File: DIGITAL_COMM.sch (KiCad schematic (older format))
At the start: 7 parts, among them U4 MCP3004, U5 TC77

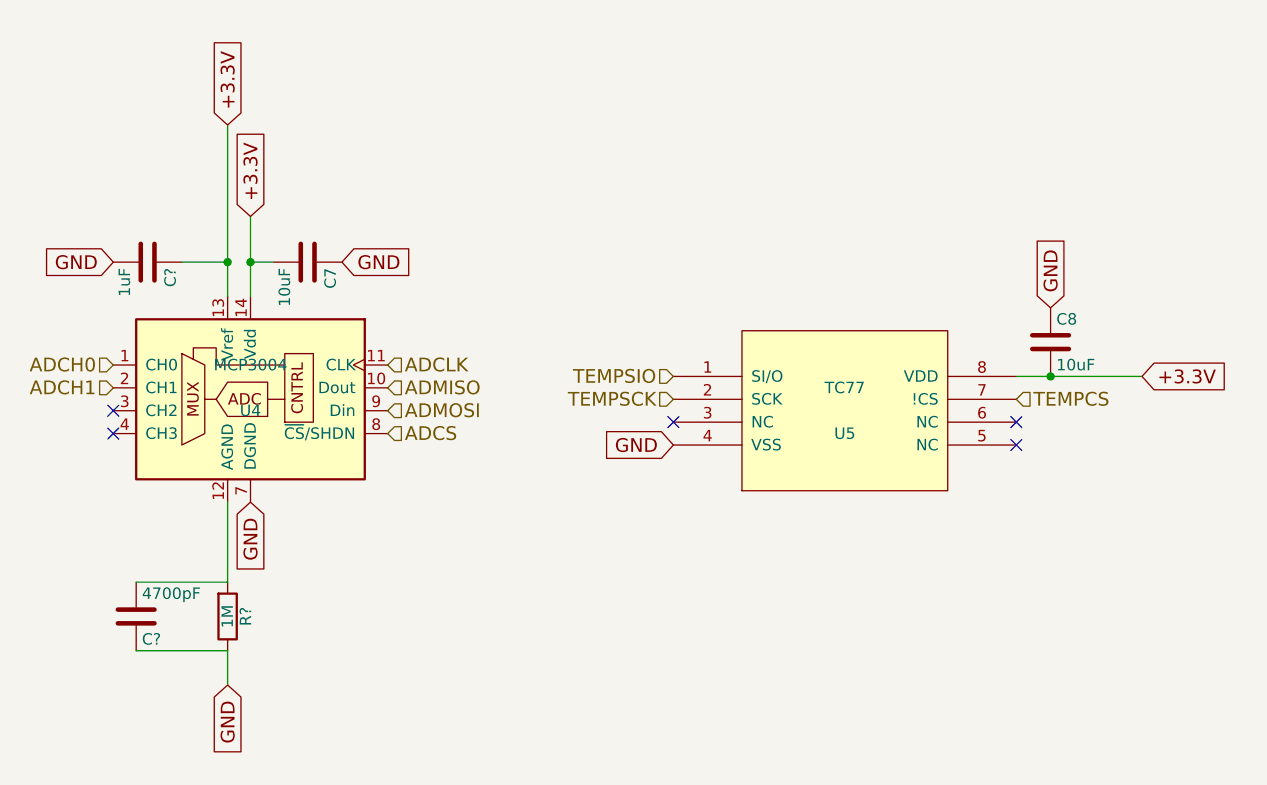
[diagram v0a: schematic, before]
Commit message: this version contains the datasheets and the footprints of the parts
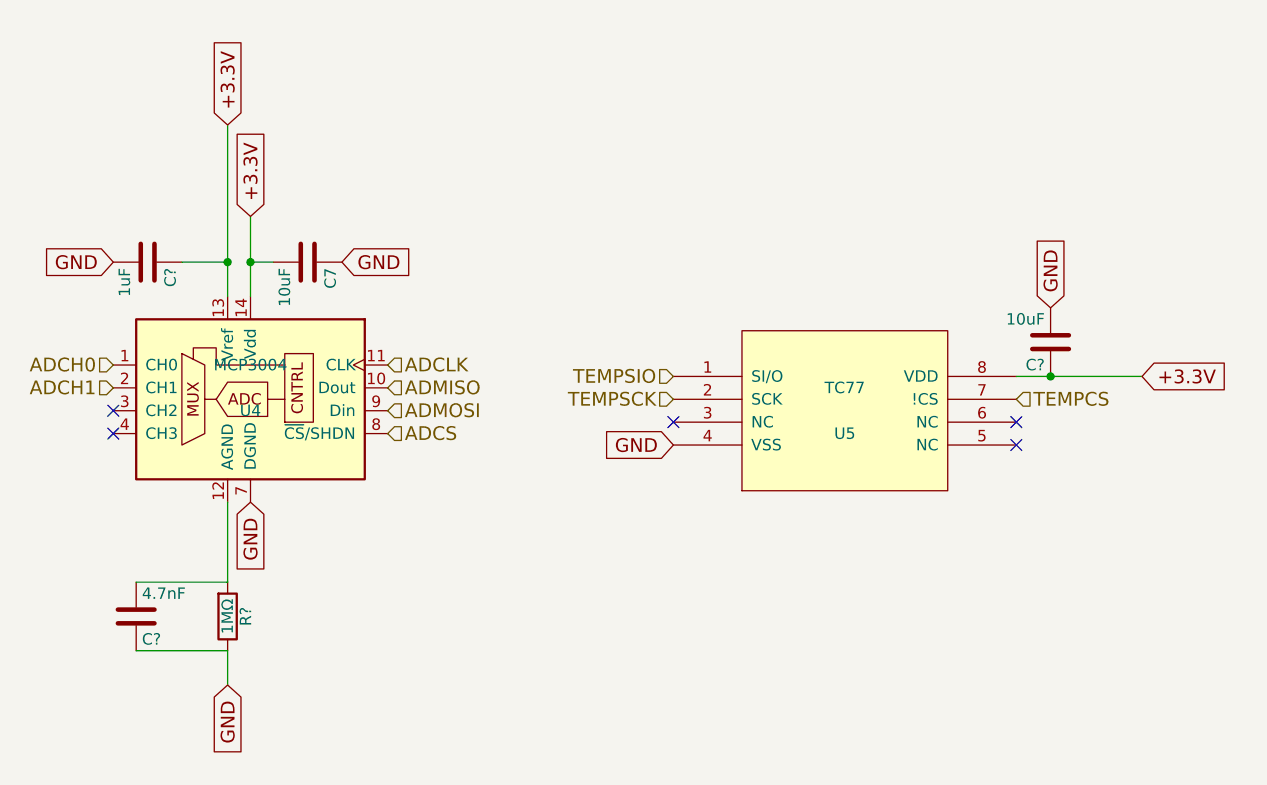
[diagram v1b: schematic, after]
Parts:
- removed C8: 10uF, Capacitors_SMD:C_1206_HandSoldering, symbol C
- removed C?: 4700pF, symbol C
- added C?: 4.7nF, Capacitors_SMD:C_0603_HandSoldering, symbol C
- added C?: 10uF, Capacitors_SMD:C_0603_HandSoldering, symbol C
- C7: footprint Capacitors_SMD:C_1206_HandSoldering -> Capacitors_SMD:C_0603_HandSoldering; avx (none) -> http://hu.farnell.com/avx/06036d106mat2a/cap-mlcc-x5r-10uf-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
- C?: footprint (none) -> Capacitors_SMD:C_0603_HandSoldering
- R?: value 1M -> 1MΩ; footprint (none) -> Resistors_SMD:R_0603_HandSoldering
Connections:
- net +3.3V: now also C?.1
- net GND: now also C?.1, C?.2
- net at R?.2, U4.12 (AGND): now also C?.2
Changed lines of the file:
@@
-$EndComp
-$Comp
-L C C8
-U 1 1 561C1F39
-P 7050 2400
-F 0 "C8" H 7075 2500 50  0000 L CNN
-F 1 "10uF" H 7075 2300 50  0000 L CNN
-F 2 "Capacitors_SMD:C_1206_HandSoldering" H 7088 2250 30  0001 C CNN
-F 3 "" H 7050 2400 60  0000 C CNN
-	1    7050 2400
-	1    0    0    -1
 $EndComp
 $Comp
@@
 F 0 "C7" H 3825 2150 50  0000 L CNN
 F 1 "10uF" H 3825 1950 50  0000 L CNN
-F 2 "Capacitors_SMD:C_1206_HandSoldering" H 3838 1900 30  0001 C CNN
-F 3 "" H 3800 2050 60  0000 C CNN
+F 2 "Capacitors_SMD:C_0603_HandSoldering" H 3838 1900 30  0001 C CNN
+F 3 "http://hu.farnell.com/murata/grm188r60g106me47d/cap-mlcc-x5r-10uf-4v-0603/dp/2688517" H 3800 2050 60  0001 C CNN
+F 4 "http://hu.farnell.com/avx/06036d106mat2a/cap-mlcc-x5r-10uf-6-3v-0603/dp/1833804" H 3800 2050 60  0001 C CNN "avx"
 	1    3800 2050
 	0    1    1    0
@@
 GND
 $Comp
-L C C?
-U 1 1 59A60423
-P 3050 3600
-F 0 "C?" H 3075 3700 50  0000 L CNN
-F 1 "4700pF" H 3075 3500 50  0000 L CNN
-F 2 "" H 3088 3450 50  0001 C CNN
-F 3 "" H 3050 3600 50  0001 C CNN
-	1    3050 3600
-	1    0    0    1
-$EndComp
-$Comp
 L R R?
 U 1 1 59A6042A
 P 3450 3600
 F 0 "R?" V 3530 3600 50  0000 C CNN
-F 1 "1M" V 3450 3600 50  0000 C CNN
-F 2 "" V 3380 3600 50  0001 C CNN
-F 3 "" H 3450 3600 50  0001 C CNN
+F 1 "1MΩ" V 3450 3600 50  0000 C CNN
+F 2 "Resistors_SMD:R_0603_HandSoldering" V 3380 3600 50  0001 C CNN
+F 3 "http://hu.farnell.com/multicomp/mcwr06x1004ftl/res-thick-film-1m-1-0-1w-0603/dp/2447285" H 3450 3600 50  0001 C CNN
 	1    3450 3600
 	1    0    0    1
@@
 F 0 "C?" H 3125 2150 50  0000 L CNN
 F 1 "1uF" H 3125 1950 50  0000 L CNN
-F 2 "" H 3138 1900 50  0001 C CNN
-F 3 "" H 3100 2050 50  0001 C CNN
+F 2 "Capacitors_SMD:C_0603_HandSoldering" H 3138 1900 50  0001 C CNN
+F 3 "http://hu.farnell.com/avx/0603zd105kat2a/cap-mlcc-x5r-1uf-10v-0603/dp/1327684" H 3100 2050 50  0001 C CNN
 	1    3100 2050
 	0    1    1    0
@@
 NoConn ~ 2950 2800
 NoConn ~ 2950 2700
+$Comp
+L C C?
+U 1 1 59A7620E
+P 7050 2400
+F 0 "C?" H 7075 2500 50  0000 L CNN
+F 1 "10uF" H 7075 2300 50  0000 L CNN
+F 2 "Capacitors_SMD:C_0603_HandSoldering" H 7088 2250 30  0001 C CNN
+F 3 "http://hu.farnell.com/murata/grm188r60g106me47d/cap-mlcc-x5r-10uf-4v-0603/dp/2688517" H 7050 2400 60  0001 C CNN
+F 4 "http://hu.farnell.com/avx/06036d106mat2a/cap-mlcc-x5r-10uf-6-3v-0603/dp/1833804" H 7050 2400 60  0001 C CNN "avx"
+	1    7050 2400
+	-1   0    0    1
+$EndComp
+$Comp
+L C C?
+U 1 1 59A6A163
+P 3050 3600
+F 0 "C?" H 3075 3700 50  0000 L CNN
+F 1 "4.7nF" H 3075 3500 50  0000 L CNN
+F 2 "Capacitors_SMD:C_0603_HandSoldering" H 3088 3450 50  0001 C CNN
+F 3 "http://hu.farnell.com/avx/06035c472kat2a/cap-mlcc-x7r-4-7nf-50v-0603/dp/317263" H 3050 3600 50  0001 C CNN
+	1    3050 3600
+	1    0    0    1
+$EndComp
 $EndSCHEMATC

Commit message: some issues fixed by the bugfixer; formal verification needed
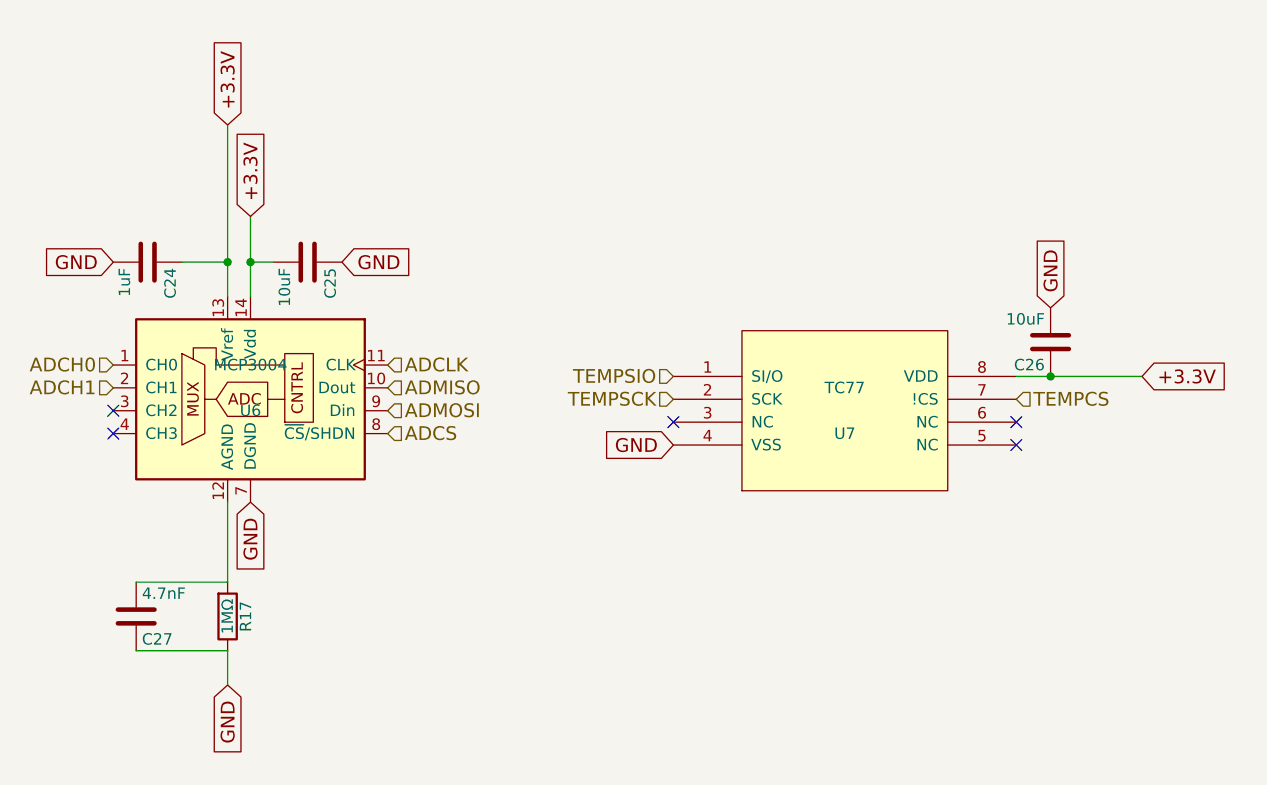
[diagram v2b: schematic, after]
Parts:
- gave numbers to parts that had none: 4
- renumbered C7 to C25, U4 to U6, U5 to U7
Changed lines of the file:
@@
 $EndDescr
 $Comp
-L MCP3004 U4
+L MCP3004 U6
 U 1 1 561B93E7
 P 3550 2600
-F 0 "U4" H 3550 2500 50  0000 C CNN
+F 0 "U6" H 3550 2500 50  0000 C CNN
 F 1 "MCP3004" H 3550 2700 50  0000 C CNN
 F 2 "Housings_SOIC:SOIC-14_3.9x8.7mm_Pitch1.27mm" H 3550 2600 50  0001 C CNN
@@
 $EndComp
 $Comp
-L TC77 U5
+L TC77 U7
 U 1 1 561B943C
 P 6150 2700
-F 0 "U5" H 6150 2600 50  0000 C CNN
+F 0 "U7" H 6150 2600 50  0000 C CNN
 F 1 "TC77" H 6150 2800 50  0000 C CNN
 F 2 "Housings_SOIC:SOIC-8_3.9x4.9mm_Pitch1.27mm" H 6150 2700 50  0001 C CNN
@@
 $EndComp
 $Comp
-L C C7
+L C C25
 U 1 1 561C1FA8
 P 3800 2050
-F 0 "C7" H 3825 2150 50  0000 L CNN
+F 0 "C25" H 3825 2150 50  0000 L CNN
 F 1 "10uF" H 3825 1950 50  0000 L CNN
 F 2 "Capacitors_SMD:C_0603_HandSoldering" H 3838 1900 30  0001 C CNN
@@
 GND
 $Comp
-L R R?
+L R R17
 U 1 1 59A6042A
 P 3450 3600
-F 0 "R?" V 3530 3600 50  0000 C CNN
+F 0 "R17" V 3530 3600 50  0000 C CNN
 F 1 "1MΩ" V 3450 3600 50  0000 C CNN
 F 2 "Resistors_SMD:R_0603_HandSoldering" V 3380 3600 50  0001 C CNN
@@
 	3450 3100 3450 3450
 $Comp
-L C C?
+L C C24
 U 1 1 59A609F8
 P 3100 2050
-F 0 "C?" H 3125 2150 50  0000 L CNN
+F 0 "C24" H 3125 2150 50  0000 L CNN
 F 1 "1uF" H 3125 1950 50  0000 L CNN
 F 2 "Capacitors_SMD:C_0603_HandSoldering" H 3138 1900 50  0001 C CNN
@@
 NoConn ~ 2950 2700
 $Comp
-L C C?
+L C C26
 U 1 1 59A7620E
 P 7050 2400
-F 0 "C?" H 7075 2500 50  0000 L CNN
+F 0 "C26" H 7075 2500 50  0000 L CNN
 F 1 "10uF" H 7075 2300 50  0000 L CNN
 F 2 "Capacitors_SMD:C_0603_HandSoldering" H 7088 2250 30  0001 C CNN
@@
 $EndComp
 $Comp
-L C C?
+L C C27
 U 1 1 59A6A163
 P 3050 3600
-F 0 "C?" H 3075 3700 50  0000 L CNN
+F 0 "C27" H 3075 3700 50  0000 L CNN
 F 1 "4.7nF" H 3075 3500 50  0000 L CNN
 F 2 "Capacitors_SMD:C_0603_HandSoldering" H 3088 3450 50  0001 C CNN

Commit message: part numbers generated;
pcb generation started
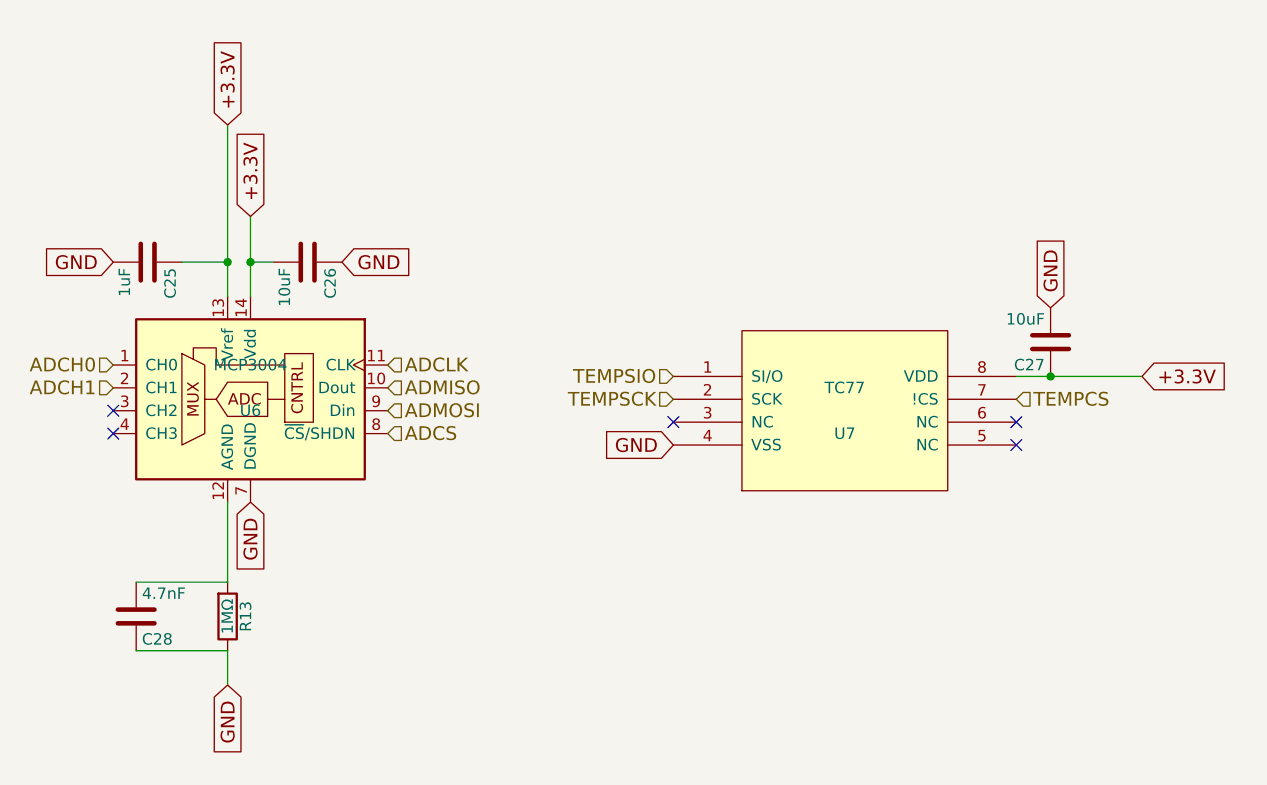
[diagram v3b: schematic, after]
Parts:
- renumbered C24 to C25, C25 to C26, C26 to C27, C27 to C28, R17 to R13
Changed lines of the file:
@@
 $EndComp
 $Comp
-L C C25
+L C C26
 U 1 1 561C1FA8
 P 3800 2050
-F 0 "C25" H 3825 2150 50  0000 L CNN
+F 0 "C26" H 3825 2150 50  0000 L CNN
 F 1 "10uF" H 3825 1950 50  0000 L CNN
 F 2 "Capacitors_SMD:C_0603_HandSoldering" H 3838 1900 30  0001 C CNN
@@
 GND
 $Comp
-L R R17
+L R R13
 U 1 1 59A6042A
 P 3450 3600
-F 0 "R17" V 3530 3600 50  0000 C CNN
+F 0 "R13" V 3530 3600 50  0000 C CNN
 F 1 "1MΩ" V 3450 3600 50  0000 C CNN
 F 2 "Resistors_SMD:R_0603_HandSoldering" V 3380 3600 50  0001 C CNN
@@
 	3450 3100 3450 3450
 $Comp
-L C C24
+L C C25
 U 1 1 59A609F8
 P 3100 2050
-F 0 "C24" H 3125 2150 50  0000 L CNN
+F 0 "C25" H 3125 2150 50  0000 L CNN
 F 1 "1uF" H 3125 1950 50  0000 L CNN
 F 2 "Capacitors_SMD:C_0603_HandSoldering" H 3138 1900 50  0001 C CNN
@@
 NoConn ~ 2950 2700
 $Comp
-L C C26
+L C C27
 U 1 1 59A7620E
 P 7050 2400
-F 0 "C26" H 7075 2500 50  0000 L CNN
+F 0 "C27" H 7075 2500 50  0000 L CNN
 F 1 "10uF" H 7075 2300 50  0000 L CNN
 F 2 "Capacitors_SMD:C_0603_HandSoldering" H 7088 2250 30  0001 C CNN
@@
 $EndComp
 $Comp
-L C C27
+L C C28
 U 1 1 59A6A163
 P 3050 3600
-F 0 "C27" H 3075 3700 50  0000 L CNN
+F 0 "C28" H 3075 3700 50  0000 L CNN
 F 1 "4.7nF" H 3075 3500 50  0000 L CNN
 F 2 "Capacitors_SMD:C_0603_HandSoldering" H 3088 3450 50  0001 C CNN
